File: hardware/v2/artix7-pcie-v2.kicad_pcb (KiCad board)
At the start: 4 copper layers, 60 x 51 mm, 187 parts, among them J1 Conn_02x20_Odd_Even, J10 USB_B_Micro, J2 Conn_02x20_Odd_Even, J4 USB3_A, J5 USB3_A_AS_PCIE, J6 JTAG, J7 Conn_01x02, J8 SER, SW1 PROG, SW2 USER, U1 XC7A75T-FGG484, U10 TPS74701DRCR, U2 MX25L51245GZ2I-10G, U3 TLV62569DBVR, U4 5P49V6965A000NLGI, U5 TLV62569PDDCR, U6 TLV62569DBVR, U7 TLV62569DBVR, U8 TLV62569DBVR, U9 TPS74701DRCR, X1 25MHz/10pF

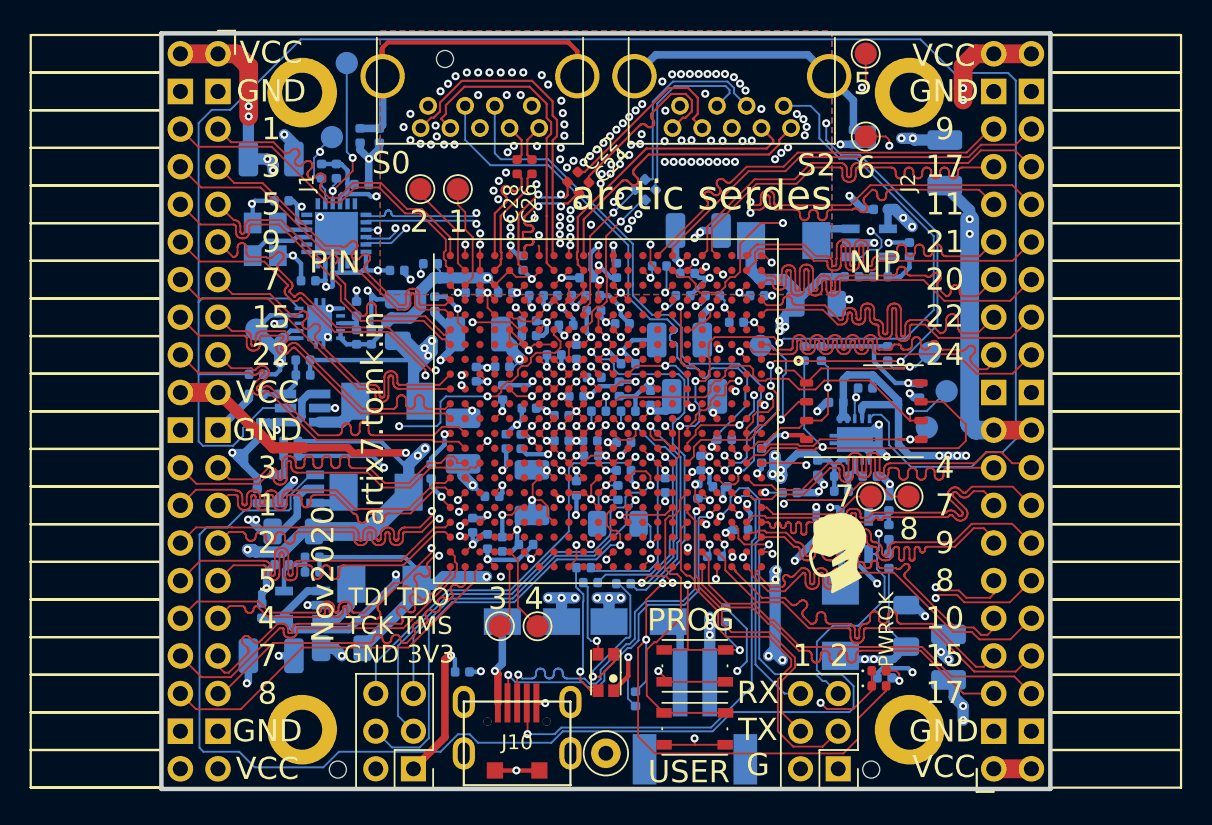
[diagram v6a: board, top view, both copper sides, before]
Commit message: hardware: minor fixes to v2 for Nov2020 run
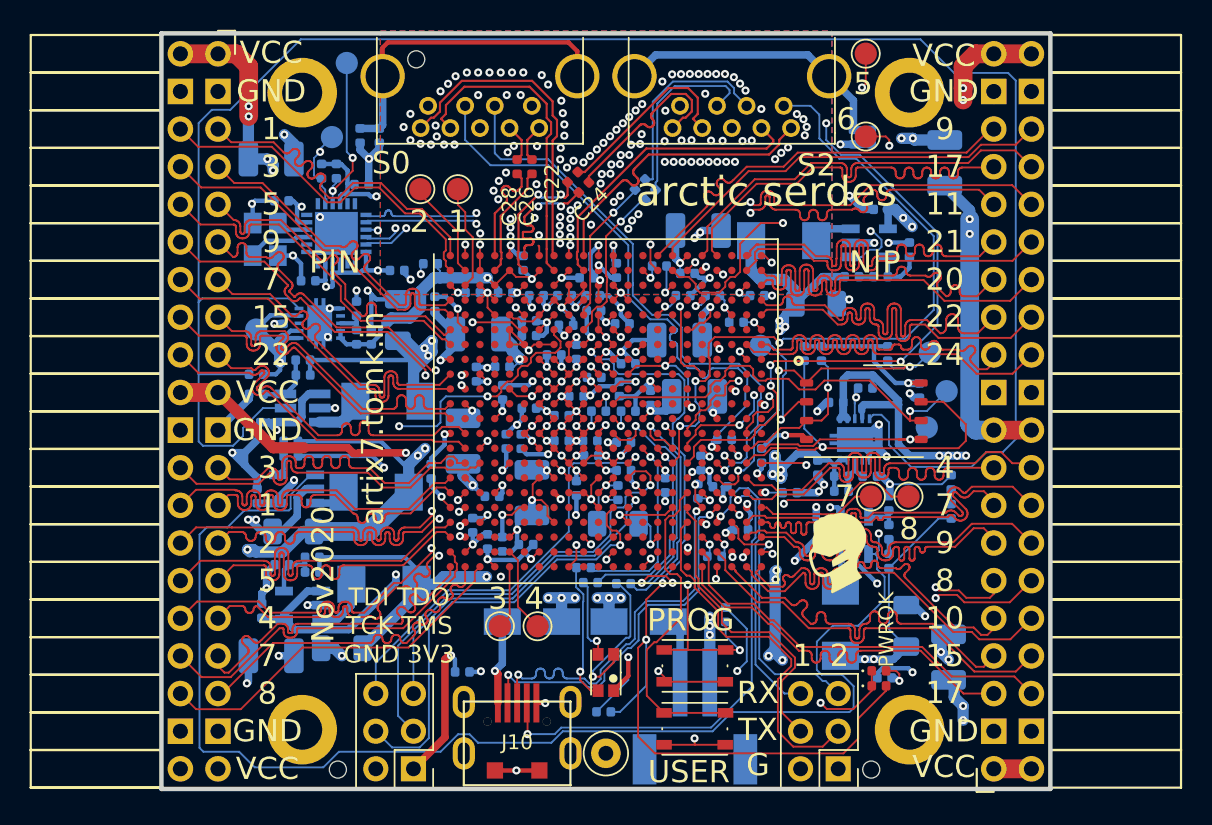
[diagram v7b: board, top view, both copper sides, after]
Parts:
- added D6: PWR, tom-opto:LED_0402_1005Metric, B.Cu at (164.4, 91.6)
- added R4: 4.7k/5%, tom-passives:R_0402_1005Metric, B.Cu at (164.4, 93.6)
- moved R1 2.32 mm to (140.9, 107.1), turned to 0 degrees
- moved H3 1.94 mm to (128.3, 63.1)
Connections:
- U1 pad A13: (no net) -> Net-(U1-PadA13)
- U1 pad A14: (no net) -> Net-(U1-PadA14)
- U1 pad A20: (no net) -> Net-(U1-PadA20)
- U1 pad AA10: (no net) -> Net-(U1-PadAA10)
- U1 pad AA11: (no net) -> Net-(U1-PadAA11)
- U1 pad AA13: (no net) -> Net-(U1-PadAA13)
- U1 pad AA14: (no net) -> Net-(U1-PadAA14)
- U1 pad AA15: (no net) -> Net-(U1-PadAA15)
- U1 pad AA16: (no net) -> Net-(U1-PadAA16)
- U1 pad AA3: (no net) -> Net-(U1-PadAA3)
- U1 pad AA4: (no net) -> Net-(U1-PadAA4)
- U1 pad AA6: (no net) -> Net-(U1-PadAA6)
- U1 pad AA8: (no net) -> Net-(U1-PadAA8)
- U1 pad AA9: (no net) -> Net-(U1-PadAA9)
- U1 pad AB10: (no net) -> Net-(U1-PadAB10)
- U1 pad AB11: (no net) -> Net-(U1-PadAB11)
- U1 pad AB12: (no net) -> Net-(U1-PadAB12)
- U1 pad AB13: (no net) -> Net-(U1-PadAB13)
- U1 pad AB15: (no net) -> Net-(U1-PadAB15)
- U1 pad AB16: (no net) -> Net-(U1-PadAB16)
- U1 pad AB17: (no net) -> Net-(U1-PadAB17)
- U1 pad AB6: (no net) -> Net-(U1-PadAB6)
- U1 pad AB7: (no net) -> Net-(U1-PadAB7)
- U1 pad AB8: (no net) -> Net-(U1-PadAB8)
- U1 pad B13: (no net) -> Net-(U1-PadB13)
- U1 pad B20: (no net) -> Net-(U1-PadB20)
- U1 pad C13: (no net) -> Net-(U1-PadC13)
- U1 pad C14: (no net) -> Net-(U1-PadC14)
- U1 pad C15: (no net) -> Net-(U1-PadC15)
- U1 pad C17: (no net) -> Net-(U1-PadC17)
- U1 pad C18: (no net) -> Net-(U1-PadC18)
- U1 pad C19: (no net) -> Net-(U1-PadC19)
- U1 pad C20: (no net) -> Net-(U1-PadC20)
- U1 pad C5: (no net) -> Net-(U1-PadC5)
- U1 pad C7: (no net) -> Net-(U1-PadC7)
- U1 pad D14: (no net) -> Net-(U1-PadD14)
- U1 pad D15: (no net) -> Net-(U1-PadD15)
- U1 pad D16: (no net) -> Net-(U1-PadD16)
- U1 pad D17: (no net) -> Net-(U1-PadD17)
- U1 pad D19: (no net) -> Net-(U1-PadD19)
- U1 pad D2: (no net) -> Net-(U1-PadD2)
- U1 pad D20: (no net) -> Net-(U1-PadD20)
- U1 pad D21: (no net) -> Net-(U1-PadD21)
- U1 pad D5: (no net) -> Net-(U1-PadD5)
- U1 pad D7: (no net) -> Net-(U1-PadD7)
- U1 pad E13: (no net) -> Net-(U1-PadE13)
- U1 pad E14: (no net) -> Net-(U1-PadE14)
- U1 pad E16: (no net) -> Net-(U1-PadE16)
- U1 pad E17: (no net) -> Net-(U1-PadE17)
- U1 pad E18: (no net) -> Net-(U1-PadE18)
- U1 pad E19: (no net) -> Net-(U1-PadE19)
- U1 pad E2: (no net) -> Net-(U1-PadE2)
- U1 pad E21: (no net) -> Net-(U1-PadE21)
- U1 pad E3: (no net) -> Net-(U1-PadE3)
- U1 pad F13: (no net) -> Net-(U1-PadF13)
- U1 pad F14: (no net) -> Net-(U1-PadF14)
- U1 pad F15: (no net) -> Net-(U1-PadF15)
- U1 pad F16: (no net) -> Net-(U1-PadF16)
- U1 pad F18: (no net) -> Net-(U1-PadF18)
- U1 pad F19: (no net) -> Net-(U1-PadF19)
- U1 pad F20: (no net) -> Net-(U1-PadF20)
- U1 pad F21: (no net) -> Net-(U1-PadF21)
- U1 pad F3: (no net) -> Net-(U1-PadF3)
- U1 pad F4: (no net) -> Net-(U1-PadF4)
- U1 pad G13: (no net) -> Net-(U1-PadG13)
- U1 pad G15: (no net) -> Net-(U1-PadG15)
- U1 pad G16: (no net) -> Net-(U1-PadG16)
- U1 pad G17: (no net) -> Net-(U1-PadG17)
- U1 pad G18: (no net) -> Net-(U1-PadG18)
- U1 pad G2: (no net) -> Net-(U1-PadG2)
- U1 pad G20: (no net) -> Net-(U1-PadG20)
- U1 pad G3: (no net) -> Net-(U1-PadG3)
- U1 pad G4: (no net) -> Net-(U1-PadG4)
- U1 pad H13: (no net) -> Net-(U1-PadH13)
- U1 pad H14: (no net) -> Net-(U1-PadH14)
- U1 pad H15: (no net) -> Net-(U1-PadH15)
- U1 pad H17: (no net) -> Net-(U1-PadH17)
- U1 pad H18: (no net) -> Net-(U1-PadH18)
- U1 pad H19: (no net) -> Net-(U1-PadH19)
- U1 pad H2: (no net) -> Net-(U1-PadH2)
- U1 pad H20: (no net) -> Net-(U1-PadH20)
- U1 pad H22: (no net) -> Net-(U1-PadH22)
- U1 pad H3: (no net) -> Net-(U1-PadH3)
- U1 pad H4: (no net) -> Net-(U1-PadH4)
- U1 pad H5: (no net) -> Net-(U1-PadH5)
- U1 pad J14: (no net) -> Net-(U1-PadJ14)
- U1 pad J15: (no net) -> Net-(U1-PadJ15)
- U1 pad J16: (no net) -> Net-(U1-PadJ16)
- U1 pad J17: (no net) -> Net-(U1-PadJ17)
- U1 pad J19: (no net) -> Net-(U1-PadJ19)
- U1 pad J20: (no net) -> Net-(U1-PadJ20)
- U1 pad J21: (no net) -> Net-(U1-PadJ21)
- U1 pad J22: (no net) -> Net-(U1-PadJ22)
- U1 pad J4: (no net) -> Net-(U1-PadJ4)
- U1 pad J5: (no net) -> Net-(U1-PadJ5)
- U1 pad J6: (no net) -> Net-(U1-PadJ6)
- U1 pad K13: (no net) -> Net-(U1-PadK13)
- U1 pad K14: (no net) -> Net-(U1-PadK14)
- U1 pad K16: (no net) -> Net-(U1-PadK16)
- U1 pad K17: (no net) -> Net-(U1-PadK17)
- U1 pad K18: (no net) -> Net-(U1-PadK18)
- U1 pad K19: (no net) -> Net-(U1-PadK19)
- U1 pad K21: (no net) -> Net-(U1-PadK21)
- U1 pad K22: (no net) -> Net-(U1-PadK22)
- U1 pad K3: (no net) -> Net-(U1-PadK3)
- U1 pad K4: (no net) -> Net-(U1-PadK4)
- U1 pad K6: (no net) -> Net-(U1-PadK6)
- U1 pad L13: (no net) -> Net-(U1-PadL13)
- U1 pad L14: (no net) -> Net-(U1-PadL14)
- U1 pad L15: (no net) -> Net-(U1-PadL15)
- U1 pad L16: (no net) -> Net-(U1-PadL16)
- U1 pad L18: (no net) -> Net-(U1-PadL18)
- U1 pad L19: (no net) -> Net-(U1-PadL19)
- U1 pad L20: (no net) -> Net-(U1-PadL20)
- U1 pad L21: (no net) -> Net-(U1-PadL21)
- U1 pad L3: (no net) -> Net-(U1-PadL3)
- U1 pad L4: (no net) -> Net-(U1-PadL4)
- U1 pad L5: (no net) -> Net-(U1-PadL5)
- U1 pad L6: (no net) -> Net-(U1-PadL6)
- U1 pad M13: (no net) -> Net-(U1-PadM13)
- U1 pad M15: (no net) -> Net-(U1-PadM15)
- U1 pad M16: (no net) -> Net-(U1-PadM16)
- U1 pad M17: (no net) -> Net-(U1-PadM17)
- U1 pad M18: (no net) -> Net-(U1-PadM18)
- U1 pad M2: (no net) -> Net-(U1-PadM2)
- U1 pad M20: (no net) -> Net-(U1-PadM20)
- U1 pad M21: (no net) -> Net-(U1-PadM21)
- U1 pad M22: (no net) -> Net-(U1-PadM22)
- U1 pad M3: (no net) -> Net-(U1-PadM3)
- U1 pad M5: (no net) -> Net-(U1-PadM5)
- U1 pad M6: (no net) -> Net-(U1-PadM6)
- U1 pad N13: (no net) -> Net-(U1-PadN13)
- U1 pad N14: (no net) -> Net-(U1-PadN14)
- U1 pad N15: (no net) -> Net-(U1-PadN15)
- U1 pad N18: (no net) -> Net-(U1-PadN18)
- U1 pad N19: (no net) -> Net-(U1-PadN19)
- U1 pad N20: (no net) -> Net-(U1-PadN20)
- U1 pad N22: (no net) -> Net-(U1-PadN22)
- U1 pad N3: (no net) -> Net-(U1-PadN3)
- U1 pad N4: (no net) -> Net-(U1-PadN4)
- U1 pad N5: (no net) -> Net-(U1-PadN5)
- U1 pad P1: (no net) -> Net-(U1-PadP1)
- U1 pad P4: (no net) -> Net-(U1-PadP4)
- U1 pad P5: (no net) -> Net-(U1-PadP5)
- U1 pad P6: (no net) -> Net-(U1-PadP6)
- U1 pad R1: (no net) -> Net-(U1-PadR1)
- U1 pad R14: (no net) -> Net-(U1-PadR14)
- U1 pad R18: (no net) -> Net-(U1-PadR18)
- U1 pad R4: (no net) -> Net-(U1-PadR4)
- U1 pad R6: (no net) -> Net-(U1-PadR6)
- U1 pad T14: (no net) -> Net-(U1-PadT14)
- U1 pad T15: (no net) -> Net-(U1-PadT15)
- U1 pad T16: (no net) -> Net-(U1-PadT16)
- U1 pad T18: (no net) -> Net-(U1-PadT18)
- U1 pad T20: (no net) -> Net-(U1-PadT20)
- U1 pad T3: (no net) -> Net-(U1-PadT3)
- U1 pad T4: (no net) -> Net-(U1-PadT4)
- U1 pad T5: (no net) -> Net-(U1-PadT5)
- U1 pad T6: (no net) -> Net-(U1-PadT6)
- U1 pad U15: (no net) -> Net-(U1-PadU15)
- U1 pad U16: (no net) -> Net-(U1-PadU16)
- U1 pad U3: (no net) -> Net-(U1-PadU3)
- U1 pad U5: (no net) -> Net-(U1-PadU5)
- U1 pad U6: (no net) -> Net-(U1-PadU6)
- U1 pad U7: (no net) -> Net-(U1-PadU7)
- U1 pad V10: (no net) -> Net-(U1-PadV10)
- U1 pad V13: (no net) -> Net-(U1-PadV13)
- U1 pad V14: (no net) -> Net-(U1-PadV14)
- U1 pad V15: (no net) -> Net-(U1-PadV15)
- U1 pad V3: (no net) -> Net-(U1-PadV3)
- U1 pad V4: (no net) -> Net-(U1-PadV4)
- U1 pad V5: (no net) -> Net-(U1-PadV5)
- U1 pad V7: (no net) -> Net-(U1-PadV7)
- U1 pad V8: (no net) -> Net-(U1-PadV8)
- U1 pad V9: (no net) -> Net-(U1-PadV9)
- U1 pad W10: (no net) -> Net-(U1-PadW10)
- U1 pad W11: (no net) -> Net-(U1-PadW11)
- U1 pad W12: (no net) -> Net-(U1-PadW12)
- U1 pad W14: (no net) -> Net-(U1-PadW14)
- U1 pad W15: (no net) -> Net-(U1-PadW15)
- U1 pad W16: (no net) -> Net-(U1-PadW16)
- U1 pad W4: (no net) -> Net-(U1-PadW4)
- U1 pad W5: (no net) -> Net-(U1-PadW5)
- U1 pad W6: (no net) -> Net-(U1-PadW6)
- U1 pad W7: (no net) -> Net-(U1-PadW7)
- U1 pad W9: (no net) -> Net-(U1-PadW9)
- U1 pad Y11: (no net) -> Net-(U1-PadY11)
- U1 pad Y12: (no net) -> Net-(U1-PadY12)
- U1 pad Y13: (no net) -> Net-(U1-PadY13)
- U1 pad Y14: (no net) -> Net-(U1-PadY14)
- U1 pad Y16: (no net) -> Net-(U1-PadY16)
- U1 pad Y17: (no net) -> Net-(U1-PadY17)
- U1 pad Y3: (no net) -> Net-(U1-PadY3)
- U1 pad Y4: (no net) -> Net-(U1-PadY4)
- U1 pad Y6: (no net) -> Net-(U1-PadY6)
- U1 pad Y7: (no net) -> Net-(U1-PadY7)
- U1 pad Y8: (no net) -> Net-(U1-PadY8)
- U1 pad Y9: (no net) -> Net-(U1-PadY9)
- U10 pad 7: (no net) -> Net-(U10-Pad7)
- U4 pad 1: (no net) -> Net-(U4-Pad1)
- U4 pad 11: (no net) -> Net-(U4-Pad11)
- U4 pad 12: (no net) -> Net-(U4-Pad12)
- U4 pad 19: (no net) -> Net-(U4-Pad19)
- U4 pad 2: (no net) -> Net-(U4-Pad2)
- U4 pad 20: (no net) -> Net-(U4-Pad20)
- U4 pad 24: (no net) -> Net-(U4-Pad24)
- U4 pad 6: (no net) -> Net-(U4-Pad6)
- U4 pad 7: (no net) -> Net-(U4-Pad7)
- U9 pad 3: (no net) -> Net-(U9-Pad3)
- U9 pad 7: (no net) -> Net-(U9-Pad7)
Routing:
- net +3V3: track 259.8 -> 266.5 mm
- net GND: track 289.3 -> 293.7 mm
- net /DONE: track 57.9 -> 60.4 mm
- net Net-(D6-Pad2): track 0.00 -> 0.99 mm
